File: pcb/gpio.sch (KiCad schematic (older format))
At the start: 21 parts, among them J1 Micro_SD_Card_Det_Hirose_DM3AT, U2 A33, Y1 24Mhz, Y2 32.768khz

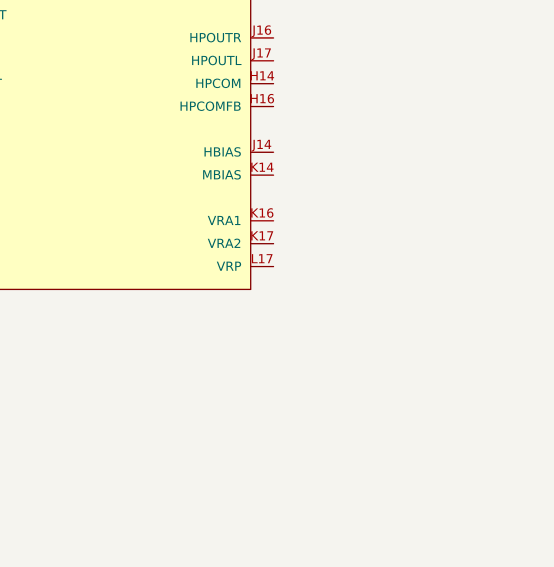
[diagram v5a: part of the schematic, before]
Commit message: Wired in some bias pins, not sure if these are needed or not?
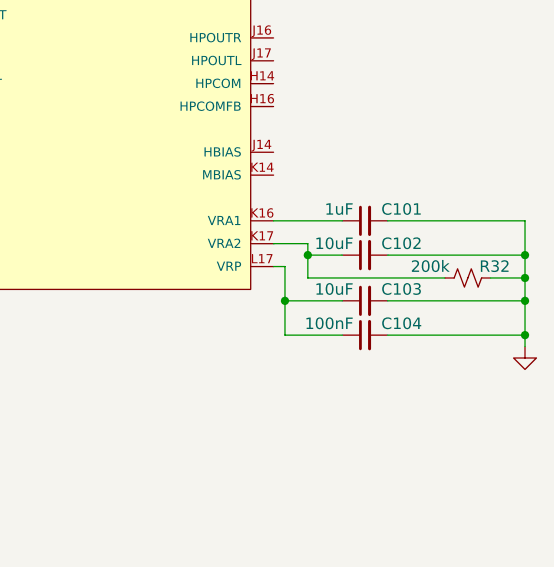
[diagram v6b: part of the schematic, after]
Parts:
- added C101: 1uF, Capacitor_SMD:C_01005_0402Metric, symbol Device:C_Small
- added C102, C103: 10uF, Capacitor_SMD:C_01005_0402Metric, symbol Device:C_Small
- added C104: 100nF, Capacitor_SMD:C_01005_0402Metric, symbol Device:C_Small
- added R32: 200k, Resistor_SMD:R_0402_1005Metric, symbol Device:R_Small_US
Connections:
- net GND: now also C101.2, C102.2, C103.2, C104.2, R32.1
- net at U2.K16 (VRA1): now also C101.1
- net at U2.K17 (VRA2): now also C102.1, R32.2
- net at U2.L17 (VRP): now also C103.1, C104.1
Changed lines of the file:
@@
 Wire Wire Line
 	7900 5400 8050 5400
+$Comp
+L Device:C_Small C?
+U 1 1 60741E44
+P 10050 5700
+AR Path="/60536DA4/60741E44" Ref="C?"  Part="1"
+AR Path="/60741E44" Ref="C?"  Part="1"
+AR Path="/6063BE69/60741E44" Ref="C101"  Part="1"
+F 0 "C101" V 10100 5450 50  0000 L CNN
+F 1 "1uF" V 10100 5750 50  0000 L CNN
+F 2 "Capacitor_SMD:C_01005_0402Metric" H 10050 5700 50  0001 C CNN
+F 3 "~" H 10050 5700 50  0001 C CNN
+	1    10050 5700
+	0    -1   -1   0
+$EndComp
+Wire Wire Line
+	9950 5700 9650 5700
+Wire Wire Line
+	10150 5700 10750 5700
+Wire Wire Line
+	10750 5700 10750 5850
+$Comp
+L Device:C_Small C?
+U 1 1 6074FC42
+P 10050 5850
+AR Path="/60536DA4/6074FC42" Ref="C?"  Part="1"
+AR Path="/6074FC42" Ref="C?"  Part="1"
+AR Path="/6063BE69/6074FC42" Ref="C102"  Part="1"
+F 0 "C102" V 10100 5600 50  0000 L CNN
+F 1 "10uF" V 10100 5900 50  0000 L CNN
+F 2 "Capacitor_SMD:C_01005_0402Metric" H 10050 5850 50  0001 C CNN
+F 3 "~" H 10050 5850 50  0001 C CNN
+	1    10050 5850
+	0    -1   -1   0
+$EndComp
+Wire Wire Line
+	9650 5800 9800 5800
+Wire Wire Line
+	9800 5800 9800 5850
+Wire Wire Line
+	10150 5850 10750 5850
+Connection ~ 10750 5850
+Wire Wire Line
+	10750 5850 10750 5950
+$Comp
+L power:GND #PWR?
+U 1 1 60761AFF
+P 10750 6250
+AR Path="/60536DA4/60761AFF" Ref="#PWR?"  Part="1"
+AR Path="/60761AFF" Ref="#PWR?"  Part="1"
+AR Path="/60A30BFF/60761AFF" Ref="#PWR?"  Part="1"
+AR Path="/6063BE69/60761AFF" Ref="#PWR077"  Part="1"
+F 0 "#PWR077" H 10750 6000 50  0001 C CNN
+F 1 "GND" V 10755 6122 50  0001 R CNN
+F 2 "" H 10750 6250 50  0001 C CNN
+F 3 "" H 10750 6250 50  0001 C CNN
+	1    10750 6250
+	1    0    0    -1
+$EndComp
+$Comp
+L Device:C_Small C?
+U 1 1 60763118
+P 10050 6050
+AR Path="/60536DA4/60763118" Ref="C?"  Part="1"
+AR Path="/60763118" Ref="C?"  Part="1"
+AR Path="/6063BE69/60763118" Ref="C103"  Part="1"
+F 0 "C103" V 10100 5800 50  0000 L CNN
+F 1 "10uF" V 10100 6100 50  0000 L CNN
+F 2 "Capacitor_SMD:C_01005_0402Metric" H 10050 6050 50  0001 C CNN
+F 3 "~" H 10050 6050 50  0001 C CNN
+	1    10050 6050
+	0    -1   -1   0
+$EndComp
+Wire Wire Line
+	9650 5900 9700 5900
+Wire Wire Line
+	9700 5900 9700 6050
+Wire Wire Line
+	9700 6050 9950 6050
+Wire Wire Line
+	10150 6050 10750 6050
+Connection ~ 10750 6050
+Wire Wire Line
+	10750 6050 10750 6200
+$Comp
+L Device:C_Small C?
+U 1 1 6076D399
+P 10050 6200
+AR Path="/60536DA4/6076D399" Ref="C?"  Part="1"
+AR Path="/6076D399" Ref="C?"  Part="1"
+AR Path="/6063BE69/6076D399" Ref="C104"  Part="1"
+F 0 "C104" V 10100 5950 50  0000 L CNN
+F 1 "100nF" V 10100 6250 50  0000 L CNN
+F 2 "Capacitor_SMD:C_01005_0402Metric" H 10050 6200 50  0001 C CNN
+F 3 "~" H 10050 6200 50  0001 C CNN
+	1    10050 6200
+	0    -1   -1   0
+$EndComp
+Wire Wire Line
+	9950 6200 9700 6200
+Wire Wire Line
+	9700 6200 9700 6050
+Connection ~ 9700 6050
+Wire Wire Line
+	10150 6200 10750 6200
+Connection ~ 10750 6200
+Wire Wire Line
+	10750 6200 10750 6250
+$Comp
+L Device:R_Small_US R?
+U 1 1 60774A6E
+P 10500 5950
+AR Path="/60536DA4/60774A6E" Ref="R?"  Part="1"
+AR Path="/60774A6E" Ref="R?"  Part="1"
+AR Path="/6063BE69/60774A6E" Ref="R32"  Part="1"
+F 0 "R32" V 10450 6000 50  0000 L CNN
+F 1 "200k" V 10450 5700 50  0000 L CNN
+F 2 "Resistor_SMD:R_0402_1005Metric" H 10500 5950 50  0001 C CNN
+F 3 "~" H 10500 5950 50  0001 C CNN
+	1    10500 5950
+	0    1    1    0
+$EndComp
+Wire Wire Line
+	10600 5950 10750 5950
+Connection ~ 10750 5950
+Wire Wire Line
+	10750 5950 10750 6050
+Wire Wire Line
+	10400 5950 9800 5950
+Wire Wire Line
+	9800 5950 9800 5850
+Connection ~ 9800 5850
+Wire Wire Line
+	9800 5850 9950 5850
 $EndSCHEMATC

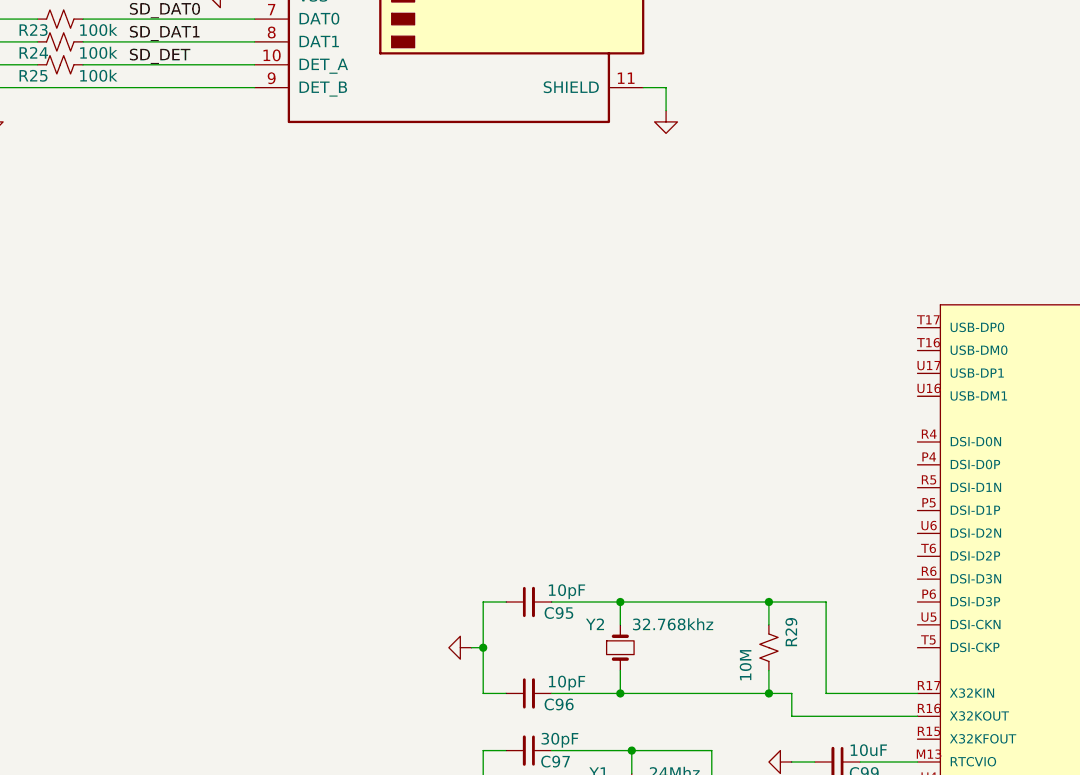
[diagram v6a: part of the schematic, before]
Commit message: Wired in the USB connectors.
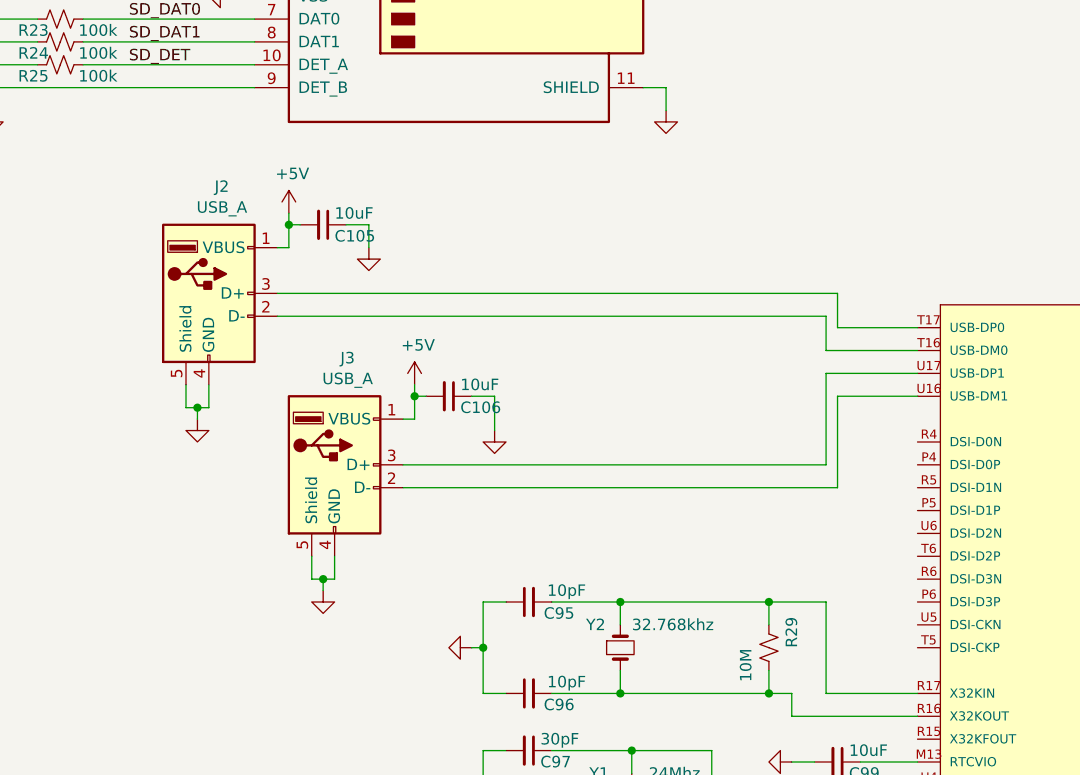
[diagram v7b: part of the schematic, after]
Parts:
- added C105, C106: 10uF, Capacitor_SMD:C_01005_0402Metric, symbol Device:C_Small
- added J2, J3: USB_A, Connector_USB:USB_A_Molex_105057_Vertical, symbol Connector:USB_A
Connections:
- net GND: now also C105.1, C106.1, J2.4 (GND), J2.5 (Shield), J3.4 (GND), J3.5 (Shield)
- net at U2.T16 (USB-DM0): now also J2.2 (D-)
- net at U2.T17 (USB-DP0): now also J2.3 (D+)
- net at U2.U16 (USB-DM1): now also J3.2 (D-)
- net at U2.U17 (USB-DP1): now also J3.3 (D+)
- new net +5V: C105.2, C106.2, J2.1 (VBUS), J3.1 (VBUS)
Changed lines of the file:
@@
 Wire Wire Line
 	9800 5850 9950 5850
+$Comp
+L Connector:USB_A J2
+U 1 1 6083640B
+P 4950 2850
+F 0 "J2" H 5007 3317 50  0000 C CNN
+F 1 "USB_A" H 5007 3226 50  0000 C CNN
+F 2 "Connector_USB:USB_A_Molex_105057_Vertical" H 5100 2800 50  0001 C CNN
+F 3 " ~" H 5100 2800 50  0001 C CNN
+F 4 "1050570001" H 4950 2850 50  0001 C CNN "Part Number"
+	1    4950 2850
+	1    0    0    -1
+$EndComp
+$Comp
+L Connector:USB_A J3
+U 1 1 60844889
+P 5500 3600
+F 0 "J3" H 5557 4067 50  0000 C CNN
+F 1 "USB_A" H 5557 3976 50  0000 C CNN
+F 2 "Connector_USB:USB_A_Molex_105057_Vertical" H 5650 3550 50  0001 C CNN
+F 3 " ~" H 5650 3550 50  0001 C CNN
+F 4 "1050570001" H 5500 3600 50  0001 C CNN "Part Number"
+	1    5500 3600
+	1    0    0    -1
+$EndComp
+Wire Wire Line
+	5250 2850 7700 2850
+Wire Wire Line
+	7700 2850 7700 3000
+Wire Wire Line
+	7700 3000 8050 3000
+Wire Wire Line
+	8050 3100 7650 3100
+Wire Wire Line
+	7650 3100 7650 2950
+Wire Wire Line
+	7650 2950 5250 2950
+Wire Wire Line
+	4850 3250 4850 3350
+Wire Wire Line
+	4850 3350 4900 3350
+Wire Wire Line
+	4950 3350 4950 3250
+$Comp
+L power:GND #PWR?
+U 1 1 608571AE
+P 4900 3400
+AR Path="/60536DA4/608571AE" Ref="#PWR?"  Part="1"
+AR Path="/608571AE" Ref="#PWR?"  Part="1"
+AR Path="/60A30BFF/608571AE" Ref="#PWR?"  Part="1"
+AR Path="/6063BE69/608571AE" Ref="#PWR078"  Part="1"
+F 0 "#PWR078" H 4900 3150 50  0001 C CNN
+F 1 "GND" V 4905 3272 50  0001 R CNN
+F 2 "" H 4900 3400 50  0001 C CNN
+F 3 "" H 4900 3400 50  0001 C CNN
+	1    4900 3400
+	1    0    0    -1
+$EndComp
+Wire Wire Line
+	4900 3400 4900 3350
+Connection ~ 4900 3350
+Wire Wire Line
+	4900 3350 4950 3350
+Wire Wire Line
+	5400 4000 5400 4100
+Wire Wire Line
+	5400 4100 5450 4100
+Wire Wire Line
+	5500 4100 5500 4000
+$Comp
+L power:GND #PWR?
+U 1 1 6086060D
+P 5450 4150
+AR Path="/60536DA4/6086060D" Ref="#PWR?"  Part="1"
+AR Path="/6086060D" Ref="#PWR?"  Part="1"
+AR Path="/60A30BFF/6086060D" Ref="#PWR?"  Part="1"
+AR Path="/6063BE69/6086060D" Ref="#PWR080"  Part="1"
+F 0 "#PWR080" H 5450 3900 50  0001 C CNN
+F 1 "GND" V 5455 4022 50  0001 R CNN
+F 2 "" H 5450 4150 50  0001 C CNN
+F 3 "" H 5450 4150 50  0001 C CNN
+	1    5450 4150
+	1    0    0    -1
+$EndComp
+Wire Wire Line
+	5450 4150 5450 4100
+Connection ~ 5450 4100
+Wire Wire Line
+	5450 4100 5500 4100
+Wire Wire Line
+	5800 3600 7650 3600
+Wire Wire Line
+	7650 3600 7650 3200
+Wire Wire Line
+	7650 3200 8050 3200
+Wire Wire Line
+	8050 3300 7700 3300
+Wire Wire Line
+	7700 3300 7700 3700
+Wire Wire Line
+	7700 3700 5800 3700
+$Comp
+L power:+5V #PWR?
+U 1 1 608AB201
+P 5300 2500
+AR Path="/60A30BFF/608AB201" Ref="#PWR?"  Part="1"
+AR Path="/6063BE69/608AB201" Ref="#PWR079"  Part="1"
+F 0 "#PWR079" H 5300 2350 50  0001 C CNN
+F 1 "+5V" H 5315 2673 50  0000 C CNN
+F 2 "" H 5300 2500 50  0001 C CNN
+F 3 "" H 5300 2500 50  0001 C CNN
+	1    5300 2500
+	1    0    0    -1
+$EndComp
+Wire Wire Line
+	5250 2650 5300 2650
+Wire Wire Line
+	5300 2500 5300 2550
+$Comp
+L power:+5V #PWR?
+U 1 1 608DBA7E
+P 5850 3250
+AR Path="/60A30BFF/608DBA7E" Ref="#PWR?"  Part="1"
+AR Path="/6063BE69/608DBA7E" Ref="#PWR082"  Part="1"
+F 0 "#PWR082" H 5850 3100 50  0001 C CNN
+F 1 "+5V" H 5865 3423 50  0000 C CNN
+F 2 "" H 5850 3250 50  0001 C CNN
+F 3 "" H 5850 3250 50  0001 C CNN
+	1    5850 3250
+	1    0    0    -1
+$EndComp
+Wire Wire Line
+	5800 3400 5850 3400
+$Comp
+L Device:C_Small C?
+U 1 1 608EED56
+P 5450 2550
+AR Path="/60536DA4/608EED56" Ref="C?"  Part="1"
+AR Path="/608EED56" Ref="C?"  Part="1"
+AR Path="/6063BE69/608EED56" Ref="C105"  Part="1"
+F 0 "C105" V 5500 2600 50  0000 L CNN
+F 1 "10uF" V 5400 2600 50  0000 L CNN
+F 2 "Capacitor_SMD:C_01005_0402Metric" H 5450 2550 50  0001 C CNN
+F 3 "~" H 5450 2550 50  0001 C CNN
+	1    5450 2550
+	0    1    1    0
+$EndComp
+$Comp
+L Device:C_Small C?
+U 1 1 608F09A6
+P 6000 3300
+AR Path="/60536DA4/608F09A6" Ref="C?"  Part="1"
+AR Path="/608F09A6" Ref="C?"  Part="1"
+AR Path="/6063BE69/608F09A6" Ref="C106"  Part="1"
+F 0 "C106" V 6050 3350 50  0000 L CNN
+F 1 "10uF" V 5950 3350 50  0000 L CNN
+F 2 "Capacitor_SMD:C_01005_0402Metric" H 6000 3300 50  0001 C CNN
+F 3 "~" H 6000 3300 50  0001 C CNN
+	1    6000 3300
+	0    1    1    0
+$EndComp
+Wire Wire Line
+	5900 3300 5850 3300
+Wire Wire Line
+	5850 3250 5850 3300
+Connection ~ 5850 3300
+Wire Wire Line
+	5850 3300 5850 3400
+Wire Wire Line
+	5350 2550 5300 2550
+Connection ~ 5300 2550
+Wire Wire Line
+	5300 2550 5300 2650
+Wire Wire Line
+	5550 2550 5650 2550
+Wire Wire Line
+	5650 2550 5650 2650
+Wire Wire Line
+	6100 3300 6200 3300
+Wire Wire Line
+	6200 3300 6200 3450
+$Comp
+L power:GND #PWR?
+U 1 1 6090816C
+P 5650 2650
+AR Path="/60536DA4/6090816C" Ref="#PWR?"  Part="1"
+AR Path="/6090816C" Ref="#PWR?"  Part="1"
+AR Path="/60A30BFF/6090816C" Ref="#PWR?"  Part="1"
+AR Path="/6063BE69/6090816C" Ref="#PWR081"  Part="1"
+F 0 "#PWR081" H 5650 2400 50  0001 C CNN
+F 1 "GND" V 5655 2522 50  0001 R CNN
+F 2 "" H 5650 2650 50  0001 C CNN
+F 3 "" H 5650 2650 50  0001 C CNN
+	1    5650 2650
+	1    0    0    -1
+$EndComp
+$Comp
+L power:GND #PWR?
+U 1 1 6090BC92
+P 6200 3450
+AR Path="/60536DA4/6090BC92" Ref="#PWR?"  Part="1"
+AR Path="/6090BC92" Ref="#PWR?"  Part="1"
+AR Path="/60A30BFF/6090BC92" Ref="#PWR?"  Part="1"
+AR Path="/6063BE69/6090BC92" Ref="#PWR083"  Part="1"
+F 0 "#PWR083" H 6200 3200 50  0001 C CNN
+F 1 "GND" V 6205 3322 50  0001 R CNN
+F 2 "" H 6200 3450 50  0001 C CNN
+F 3 "" H 6200 3450 50  0001 C CNN
+	1    6200 3450
+	1    0    0    -1
+$EndComp
 $EndSCHEMATC

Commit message: Backing up
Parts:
- added J4: Conn_01x03_Male, symbol Connector:Conn_01x03_Male
- C100, C101, C102, C103, C104, C105, C106, C93, C94, C95, C96, C97, C98, C99: footprint Capacitor_SMD:C_01005_0402Metric -> Capacitor_SMD:C_0402_1005Metric
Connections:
- net GND: now also J4.3 (Pin_3)
- net UART0_RX: now reaches U2.G16 (PB1)
- net UART0_RX: now also J4.2 (Pin_2)
- net UART0_TX: now reaches U2.G17 (PB0)
- net UART0_TX: now also J4.1 (Pin_1)
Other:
- moved on the sheet: C93, C94, J1, R20, R21, R22, R23, R24, R25, U2C
